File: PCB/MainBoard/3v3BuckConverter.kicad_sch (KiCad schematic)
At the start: 13 parts, among them U5 TPS56339DDC

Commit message: passed ERC in schematic
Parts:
- C1, C2, C6, C7, C8, C9: footprint (none) -> Capacitor_SMD:C_1206_3216Metric_Pad1.33x1.80mm_HandSolder
- JP1: footprint (none) -> Jumper:SolderJumper-2_P1.3mm_Open_TrianglePad1.0x1.5mm
- L1: footprint (none) -> Inductor_SMD:L_1206_3216Metric
- R4, R5: footprint (none) -> Resistor_THT:R_Axial_DIN0207_L6.3mm_D2.5mm_P7.62mm_Horizontal
- TP1, TP2: footprint (none) -> Connector_PinHeader_2.54mm:PinHeader_1x01_P2.54mm_Vertical
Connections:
- net +3.3V renamed +3.3V_1.2A
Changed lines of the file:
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@@
 		)
 	)
-	(hierarchical_label "12V_IN"
+	(hierarchical_label "+12V"
 		(shape input)
 		(at 76.2 88.9 180)
@@
 		)
 	)
-	(hierarchical_label "3.3V"
-		(shape input)
+	(hierarchical_label "+3.3V_1.2A"
+		(shape output)
 		(at 224.79 88.9 0)
 		(fields_autoplaced yes)
@@
 			)
 		)
-		(property "Footprint" ""
+		(property "Footprint" "Jumper:SolderJumper-2_P1.3mm_Open_TrianglePad1.0x1.5mm"
 			(at 203.2 88.9 0)
 			(effects
@@
 			)
 		)
-		(property "Footprint" ""
+		(property "Footprint" "Capacitor_SMD:C_1206_3216Metric_Pad1.33x1.80mm_HandSolder"
 			(at 169.8752 96.52 0)
 			(effects
@@
 			)
 		)
-		(property "Footprint" ""
+		(property "Footprint" "Capacitor_SMD:C_1206_3216Metric_Pad1.33x1.80mm_HandSolder"
 			(at 112.7252 97.79 0)
 			(effects
@@
 			)
 		)
-		(property "Footprint" ""
+		(property "Footprint" "Capacitor_SMD:C_1206_3216Metric_Pad1.33x1.80mm_HandSolder"
 			(at 148.2852 88.9 0)
 			(effects
@@
 			)
 		)
-		(property "Description" ""
+		(property "Description" "Power symbol creates a global label with name \"+12V\""
 			(at 116.84 86.36 0)
 			(effects
@@
 			)
 		)
-		(property "Footprint" ""
+		(property "Footprint" "Connector_PinHeader_2.54mm:PinHeader_1x01_P2.54mm_Vertical"
 			(at 194.31 116.84 0)
 			(effects
@@
 			)
 		)
-		(property "Value" "+3.3V"
+		(property "Value" "+3.3V_1.2A"
 			(at 218.44 72.39 0)
 			(effects
@@
 			)
 		)
-		(property "Footprint" ""
+		(property "Footprint" "Inductor_SMD:L_1206_3216Metric"
 			(at 162.56 88.9 0)
 			(effects
@@
 			)
 		)
-		(property "Footprint" ""
+		(property "Footprint" "Capacitor_SMD:C_1206_3216Metric_Pad1.33x1.80mm_HandSolder"
 			(at 102.5652 97.79 0)
 			(effects
@@
 			)
 		)
-		(property "Footprint" ""
+		(property "Footprint" "Resistor_THT:R_Axial_DIN0207_L6.3mm_D2.5mm_P7.62mm_Horizontal"
 			(at 189.992 105.41 90)
 			(effects
@@
 			)
 		)
-		(property "Footprint" ""
+		(property "Footprint" "Resistor_THT:R_Axial_DIN0207_L6.3mm_D2.5mm_P7.62mm_Horizontal"
 			(at 189.992 92.71 90)
 			(effects
@@
 			)
 		)
-		(property "Footprint" ""
+		(property "Footprint" "Capacitor_SMD:C_1206_3216Metric_Pad1.33x1.80mm_HandSolder"
 			(at 181.3052 96.52 0)
 			(effects
@@
 			)
 		)
-		(property "Footprint" ""
+		(property "Footprint" "Capacitor_SMD:C_1206_3216Metric_Pad1.33x1.80mm_HandSolder"
 			(at 92.4052 97.79 0)
 			(effects
@@
 			)
 		)
-		(property "Footprint" ""
+		(property "Footprint" "Connector_PinHeader_2.54mm:PinHeader_1x01_P2.54mm_Vertical"
 			(at 196.85 73.66 0)
 			(effects

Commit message: Placed Buck Converters and changed inductors to 1008
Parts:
- L1: footprint Inductor_SMD:L_1206_3216Metric -> Inductor_SMD:L_1008_2520Metric
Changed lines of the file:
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@@
 			)
 		)
-		(property "Footprint" "Inductor_SMD:L_1206_3216Metric"
+		(property "Footprint" "Inductor_SMD:L_1008_2520Metric"
 			(at 162.56 88.9 0)
 			(effects

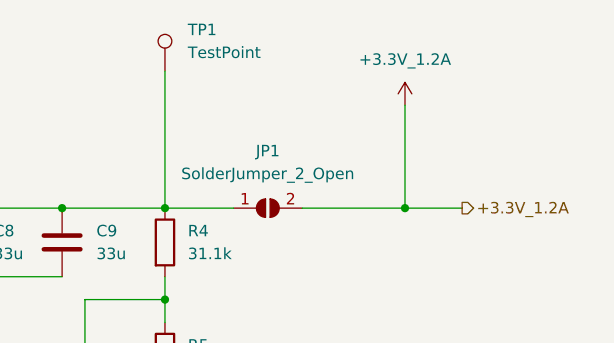
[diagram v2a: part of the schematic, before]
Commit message: adding board v2 progress
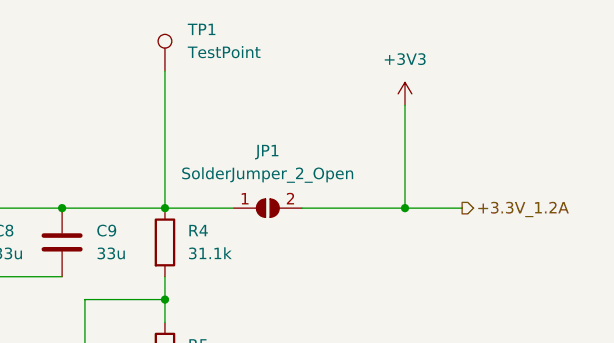
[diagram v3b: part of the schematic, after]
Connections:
- net +3.3V_1.2A renamed +3V3
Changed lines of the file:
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@@
-	)
-	(symbol
-		(lib_id "power:+3.3V")
-		(at 218.44 77.47 0)
-		(unit 1)
-		(exclude_from_sim no)
-		(in_bom yes)
-		(on_board yes)
-		(dnp no)
-		(fields_autoplaced yes)
-		(property "Reference" "#PWR038"
-			(at 218.44 81.28 0)
-			(effects
-				(font
-					(size 1.27 1.27)
-				)
-				(hide yes)
-			)
-		)
-		(property "Value" "+3.3V_1.2A"
-			(at 218.44 72.39 0)
-			(effects
-				(font
-					(size 1.27 1.27)
-				)
-			)
-		)
-		(property "Footprint" ""
-			(at 218.44 77.47 0)
-			(effects
-				(font
-					(size 1.27 1.27)
-				)
-				(hide yes)
-			)
-		)
-		(property "Datasheet" ""
-			(at 218.44 77.47 0)
-			(effects
-				(font
-					(size 1.27 1.27)
-				)
-				(hide yes)
-			)
-		)
-		(property "Description" "Power symbol creates a global label with name \"+3.3V\""
-			(at 218.44 77.47 0)
-			(effects
-				(font
-					(size 1.27 1.27)
-				)
-				(hide yes)
-			)
-		)
-		(pin "1"
-		)
-		(instances
-			(project "MainBoard"
-				(path "/ce4aa5cc-bc13-46ce-a61c-95c4be48f850/7cb6be40-ad14-404d-82c5-ced68dcd093c/87b874bb-56af-4c33-87da-99e1e73164b9"
-					(reference "#PWR038")
-					(unit 1)
-				)
-			)
-		)
 	)
 	(symbol
@@
 					(unit 1)
 				)
+			)
+		)
+	)
+	(symbol
+		(lib_id "power:+3V3")
+		(at 218.44 77.47 0)
+		(unit 1)
+		(exclude_from_sim no)
+		(in_bom yes)
+		(on_board yes)
+		(dnp no)
+		(fields_autoplaced yes)
+		(property "Reference" "#PWR038"
+			(at 218.44 81.28 0)
+			(effects
+				(font
+					(size 1.27 1.27)
+				)
+				(hide yes)
+			)
+		)
+		(property "Value" "+3V3"
+			(at 218.44 72.39 0)
+			(effects
+				(font
+					(size 1.27 1.27)
+				)
+			)
+		)
+		(property "Footprint" ""
+			(at 218.44 77.47 0)
+			(effects
+				(font
+					(size 1.27 1.27)
+				)
+				(hide yes)
+			)
+		)
+		(property "Datasheet" ""
+			(at 218.44 77.47 0)
+			(effects
+				(font
+					(size 1.27 1.27)
+				)
+				(hide yes)
+			)
+		)
+		(property "Description" "Power symbol creates a global label with name \"+3V3\""
+			(at 218.44 77.47 0)
+			(effects
+				(font
+					(size 1.27 1.27)
+				)
+				(hide yes)
+			)
+		)
+		(pin "1"
+		)
+		(instances
+			(project "MainBoard"
+				(path "/ce4aa5cc-bc13-46ce-a61c-95c4be48f850/7cb6be40-ad14-404d-82c5-ced68dcd093c/87b874bb-56af-4c33-87da-99e1e73164b9"
+					(reference "#PWR038")
+					(unit 1)
+				)
